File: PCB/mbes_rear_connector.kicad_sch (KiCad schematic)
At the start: 1 part

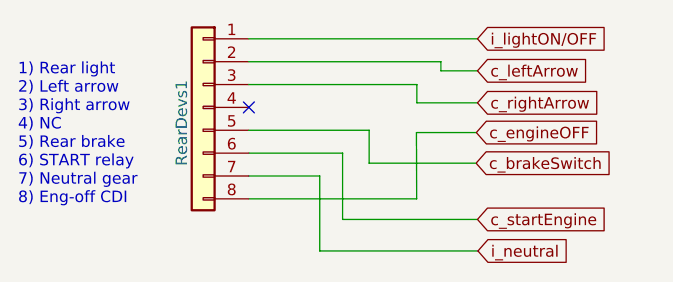
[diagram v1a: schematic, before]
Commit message: Bike-stand switch moved in the rear-connector
All connectors have been placed in one single sheet
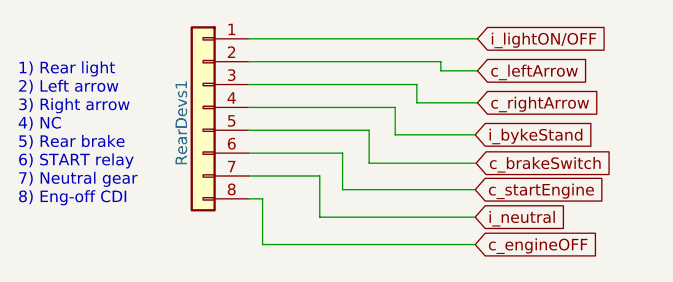
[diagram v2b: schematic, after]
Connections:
- net i_bykeStand: now reaches RearDevs1.4 (Pin_4)
- no-connect marks 1 -> 0
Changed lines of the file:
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@@
 		(comment 2 "Connector to the rear motorbike side services")
 	)
-	(no_connect
-		(at 72.644 57.658)
+	(wire
+		(pts
+			(xy 97.79 60.706) (xy 88.9 60.706)
+		)
+		(stroke
+			(width 0)
+			(type default)
+		)
 	)
 	(wire
@@
 	(wire
 		(pts
+			(xy 74.168 67.818) (xy 74.168 72.898)
+		)
+		(stroke
+			(width 0)
+			(type default)
+		)
+	)
+	(wire
+		(pts
 			(xy 72.644 65.278) (xy 80.518 65.278)
 		)
@@
 	(wire
 		(pts
-			(xy 83.058 62.738) (xy 83.058 70.104)
-		)
-		(stroke
-			(width 0)
-			(type default)
-		)
-	)
-	(wire
-		(pts
-			(xy 80.518 73.6092) (xy 98.0948 73.6092)
+			(xy 88.9 57.658) (xy 72.644 57.658)
+		)
+		(stroke
+			(width 0)
+			(type default)
+		)
+	)
+	(wire
+		(pts
+			(xy 74.168 67.818) (xy 72.644 67.818)
+		)
+		(stroke
+			(width 0)
+			(type default)
+		)
+	)
+	(wire
+		(pts
+			(xy 83.058 62.738) (xy 83.058 66.802)
+		)
+		(stroke
+			(width 0)
+			(type default)
+		)
+	)
+	(wire
+		(pts
+			(xy 80.518 69.85) (xy 97.79 69.85)
 		)
 		(stroke
@@
 	(wire
 		(pts
-			(xy 91.2876 67.818) (xy 91.2622 60.452)
+			(xy 88.9 60.706) (xy 88.9 57.658)
 		)
 		(stroke
@@
 	(wire
 		(pts
-			(xy 91.2622 60.452) (xy 97.917 60.452)
-		)
-		(stroke
-			(width 0)
-			(type default)
-		)
-	)
-	(wire
-		(pts
-			(xy 80.518 65.278) (xy 80.518 73.6092)
-		)
-		(stroke
-			(width 0)
-			(type default)
-		)
-	)
-	(wire
-		(pts
-			(xy 83.058 70.104) (xy 98.044 70.104)
+			(xy 80.518 65.278) (xy 80.518 69.85)
+		)
+		(stroke
+			(width 0)
+			(type default)
+		)
+	)
+	(wire
+		(pts
+			(xy 83.058 66.802) (xy 97.79 66.802)
 		)
 		(stroke
@@
 	(wire
 		(pts
-			(xy 72.644 67.818) (xy 91.2876 67.818)
+			(xy 74.168 72.898) (xy 97.79 72.898)
 		)
 		(stroke
@@
 	(global_label "c_startEngine"
 		(shape input)
-		(at 98.044 70.104 0)
-		(fields_autoplaced yes)
-		(effects
-			(font
-				(size 1.27 1.27)
-			)
-			(justify left)
-		)
-		(property "Intersheetrefs" "${INTERSHEET_REFS}"
-			(at 98.044 70.104 0)
-			(effects
-				(font
-					(size 1.27 1.27)
-				)
-				(hide yes)
-			)
-		)
-		(property "Riferimenti inter-foglio" "${INTERSHEET_REFS}"
-			(at 113.2176 70.0246 0)
+		(at 97.79 66.802 0)
+		(fields_autoplaced yes)
+		(effects
+			(font
+				(size 1.27 1.27)
+			)
+			(justify left)
+		)
+		(property "Intersheetrefs" "${INTERSHEET_REFS}"
+			(at 97.79 66.802 0)
+			(effects
+				(font
+					(size 1.27 1.27)
+				)
+				(hide yes)
+			)
+		)
+		(property "Riferimenti inter-foglio" "${INTERSHEET_REFS}"
+			(at 112.9636 66.7226 0)
+			(effects
+				(font
+					(size 1.27 1.27)
+				)
+				(justify left)
+				(hide yes)
+			)
+		)
+	)
+	(global_label "i_bykeStand"
+		(shape input)
+		(at 97.79 60.706 0)
+		(fields_autoplaced yes)
+		(effects
+			(font
+				(size 1.27 1.27)
+			)
+			(justify left)
+		)
+		(property "Intersheetrefs" "${INTERSHEET_REFS}"
+			(at 97.79 60.706 0)
+			(effects
+				(font
+					(size 1.27 1.27)
+				)
+				(hide yes)
+			)
+		)
+		(property "Riferimenti inter-foglio" "${INTERSHEET_REFS}"
+			(at 111.3912 60.6266 0)
 			(effects
 				(font
@@
 	(global_label "i_neutral"
 		(shape input)
-		(at 98.0948 73.6092 0)
-		(fields_autoplaced yes)
-		(effects
-			(font
-				(size 1.27 1.27)
-			)
-			(justify left)
-		)
-		(property "Intersheetrefs" "${INTERSHEET_REFS}"
-			(at 98.0948 73.6092 0)
-			(effects
-				(font
-					(size 1.27 1.27)
-				)
-				(hide yes)
-			)
-		)
-		(property "Riferimenti inter-foglio" "${INTERSHEET_REFS}"
-			(at 108.7931 73.5298 0)
+		(at 97.79 69.85 0)
+		(fields_autoplaced yes)
+		(effects
+			(font
+				(size 1.27 1.27)
+			)
+			(justify left)
+		)
+		(property "Intersheetrefs" "${INTERSHEET_REFS}"
+			(at 97.79 69.85 0)
+			(effects
+				(font
+					(size 1.27 1.27)
+				)
+				(hide yes)
+			)
+		)
+		(property "Riferimenti inter-foglio" "${INTERSHEET_REFS}"
+			(at 108.4883 69.7706 0)
 			(effects
 				(font
@@
 	(global_label "c_engineOFF"
 		(shape input)
-		(at 97.917 60.452 0)
-		(fields_autoplaced yes)
-		(effects
-			(font
-				(size 1.27 1.27)
-			)
-			(justify left)
-		)
-		(property "Intersheetrefs" "${INTERSHEET_REFS}"
-			(at 97.917 60.452 0)
-			(effects
-				(font
-					(size 1.27 1.27)
-				)
-				(hide yes)
-			)
-		)
-		(property "Riferimenti inter-foglio" "${INTERSHEET_REFS}"
-			(at 112.123 60.3726 0)
-			(effects
-				(font
+		(at 97.79 72.898 0)
+		(fields_autoplaced yes)
+		(effects
+			(font
+				(size 1.27 1.27)
+			)
+			(justify left)
+		)
+		(property "Intersheetrefs" "${INTERSHEET_REFS}"
+			(at 97.79 72.898 0)
+			(effects
+				(font
+					(size 1.27 1.27)
+				)
+				(hide yes)
+			)
+		)
+		(property "Riferimenti inter-foglio" "${INTERSHEET_REFS}"
+			(at 111.996 72.8186 0)
+			(effects
+				(font
